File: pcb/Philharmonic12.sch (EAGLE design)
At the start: 47 parts, among them IC1 MC68B21, IC10 74LS74N, IC2 AY-3-8910-RP, IC3 AY-3-8910-RP, IC4 AY-3-8910-RP, IC5 AY-3-8910-RP, IC6 74LS138N, IC7 74LS30N, IC8 LM386N-1, IC9 LM386N-1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

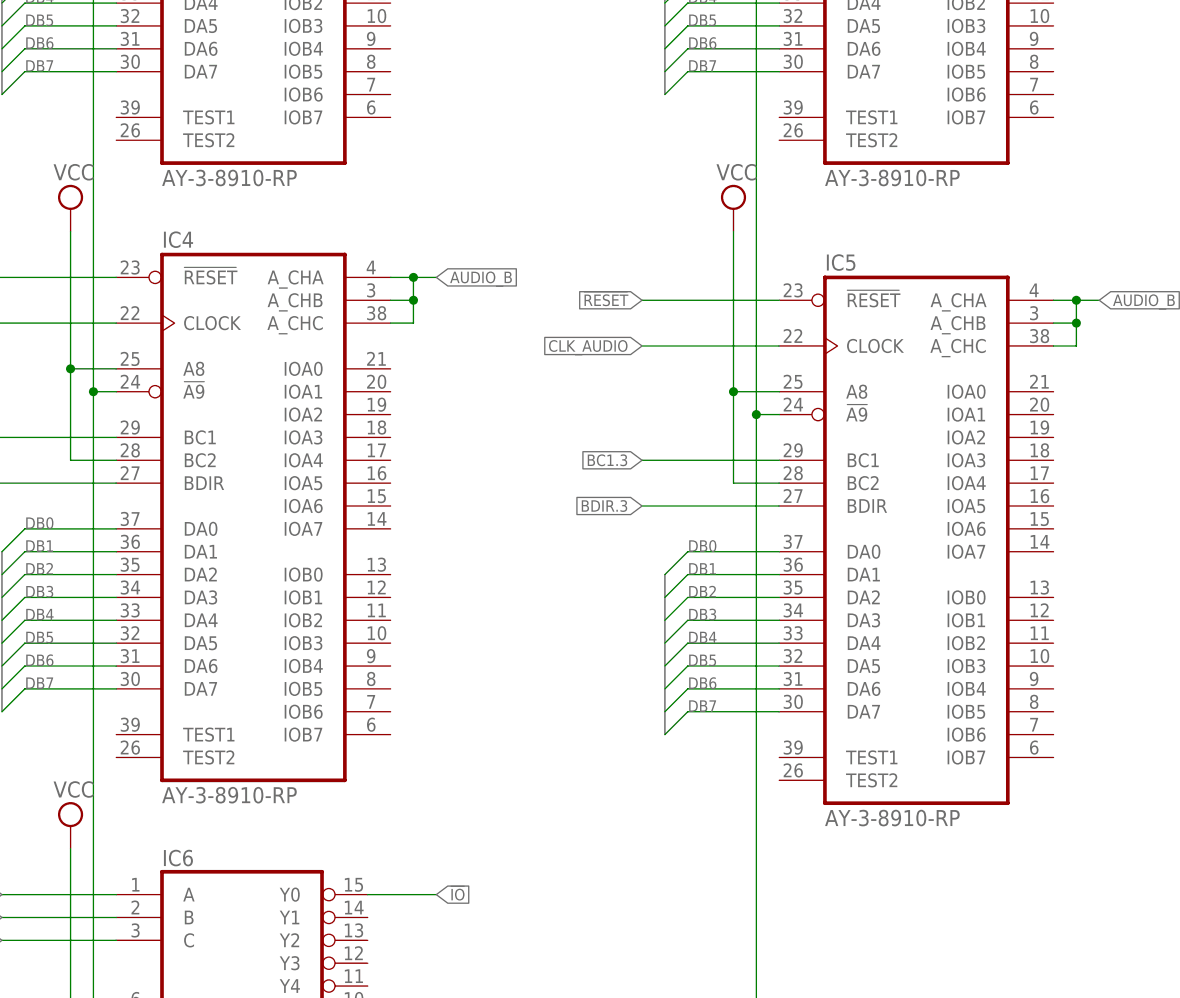
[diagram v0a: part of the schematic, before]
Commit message: Small dimension updates
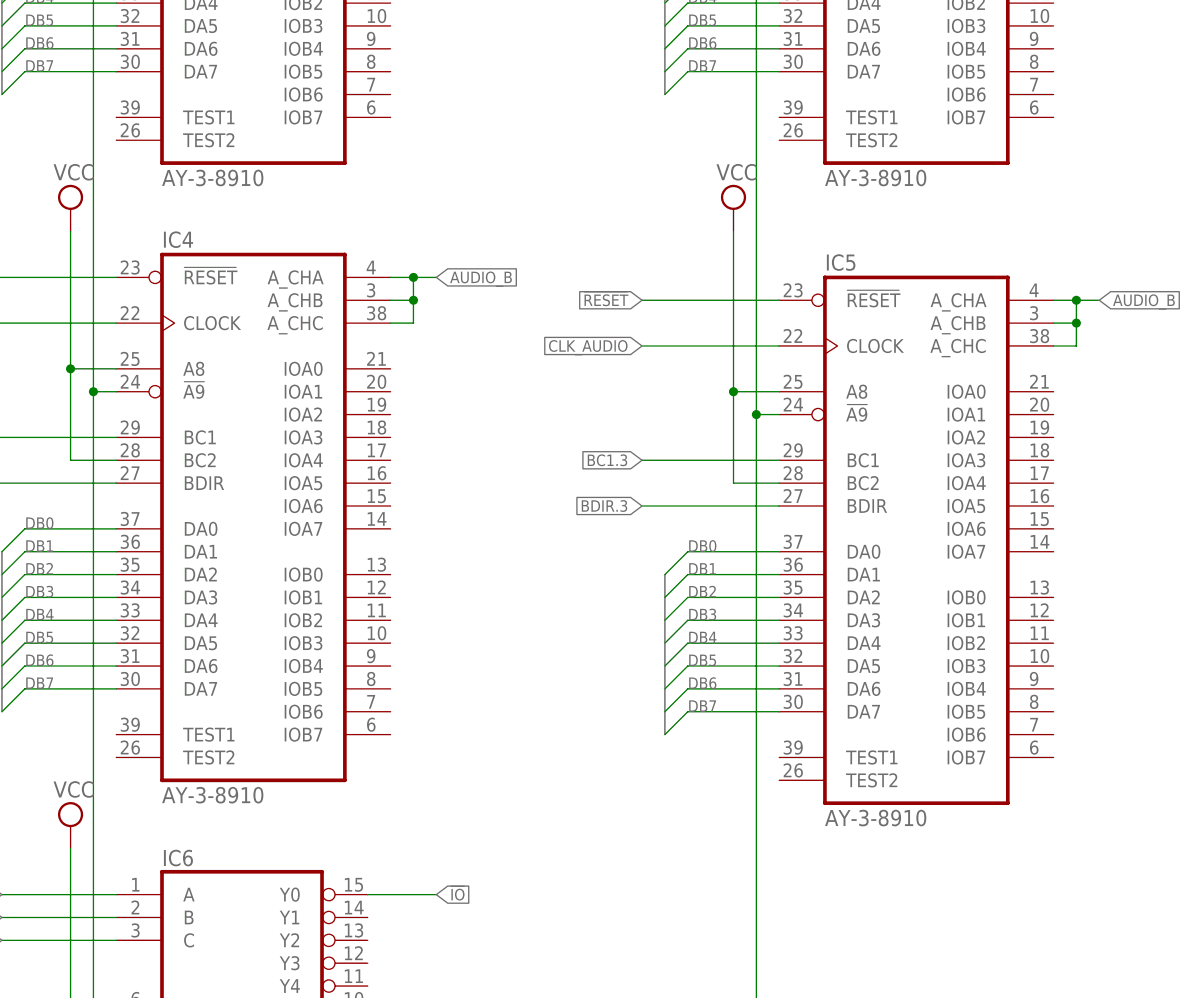
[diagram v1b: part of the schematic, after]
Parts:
- IC2, IC3, IC4, IC5: value AY-3-8910-RP -> AY-3-8910
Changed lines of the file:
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@@
 <parts>
 <part name="IC1" library="micro-motorola" deviceset="6821" device="R" value="MC68B21"/>
-<part name="IC2" library="general-instrument" deviceset="AY-3-8910" device="-RP"/>
-<part name="IC3" library="general-instrument" deviceset="AY-3-8910" device="-RP"/>
-<part name="IC4" library="general-instrument" deviceset="AY-3-8910" device="-RP"/>
-<part name="IC5" library="general-instrument" deviceset="AY-3-8910" device="-RP"/>
+<part name="IC2" library="general-instrument" deviceset="AY-3-8910" device="-RP" value="AY-3-8910"/>
+<part name="IC3" library="general-instrument" deviceset="AY-3-8910" device="-RP" value="AY-3-8910"/>
+<part name="IC4" library="general-instrument" deviceset="AY-3-8910" device="-RP" value="AY-3-8910"/>
+<part name="IC5" library="general-instrument" deviceset="AY-3-8910" device="-RP" value="AY-3-8910"/>
 <part name="X1" library="coco" deviceset="EXPANSION_PORT_COCO" device=""/>
 <part name="IC6" library="74xx-us-jlb" deviceset="74*138" device="N" technology="LS"/>

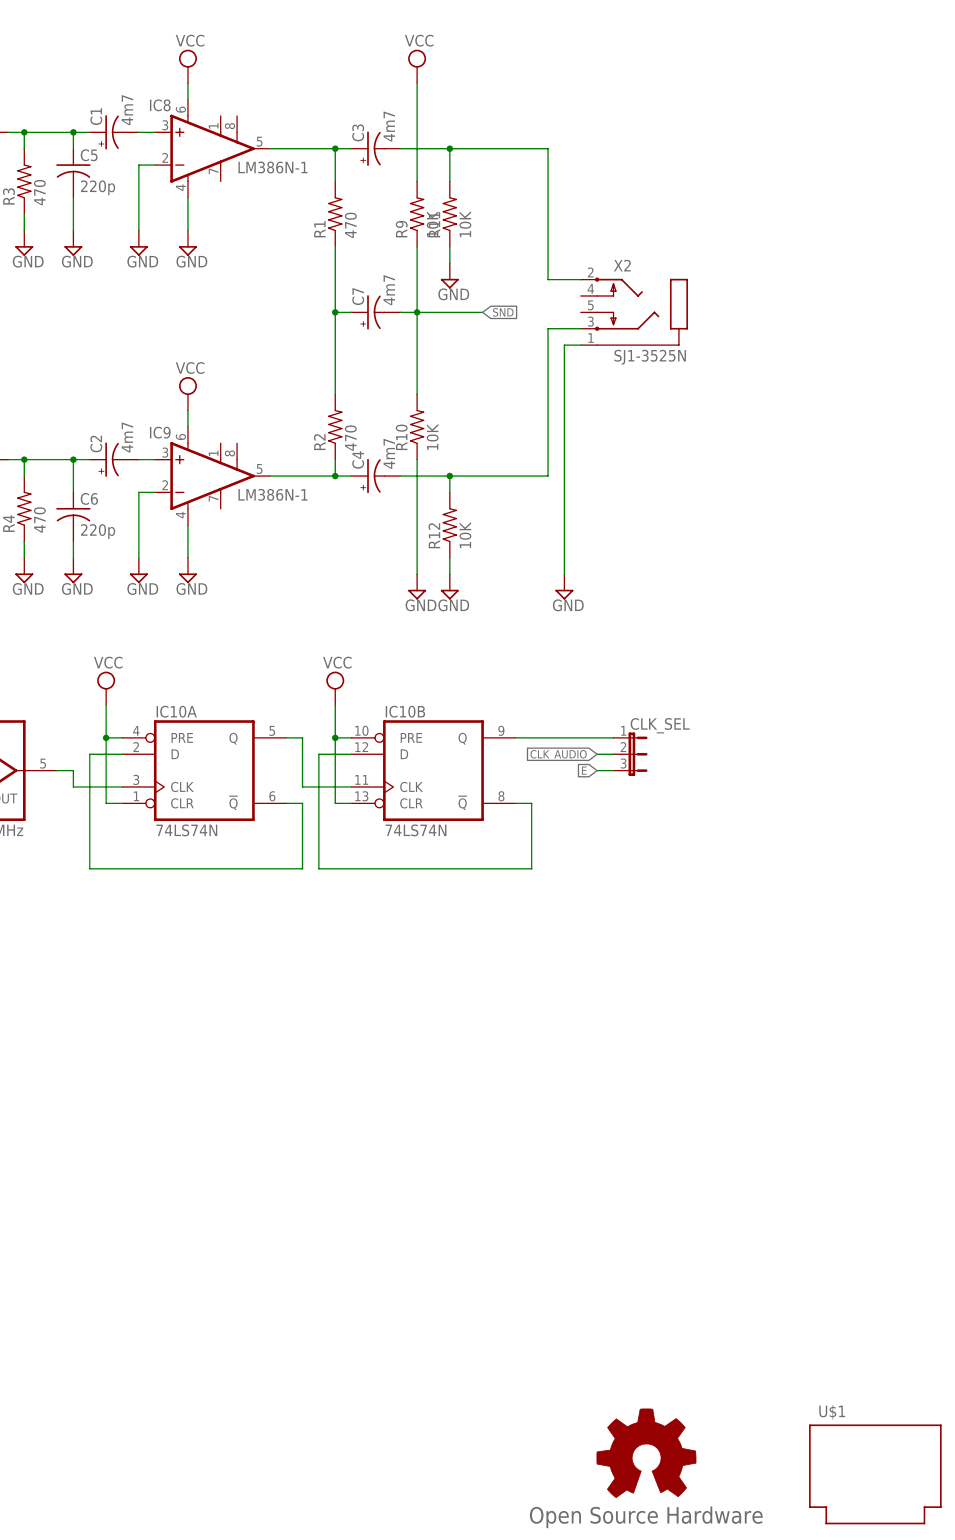
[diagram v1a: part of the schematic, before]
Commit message: Updates to schematic, Added BOM, and added sample code written by Chet Simpson
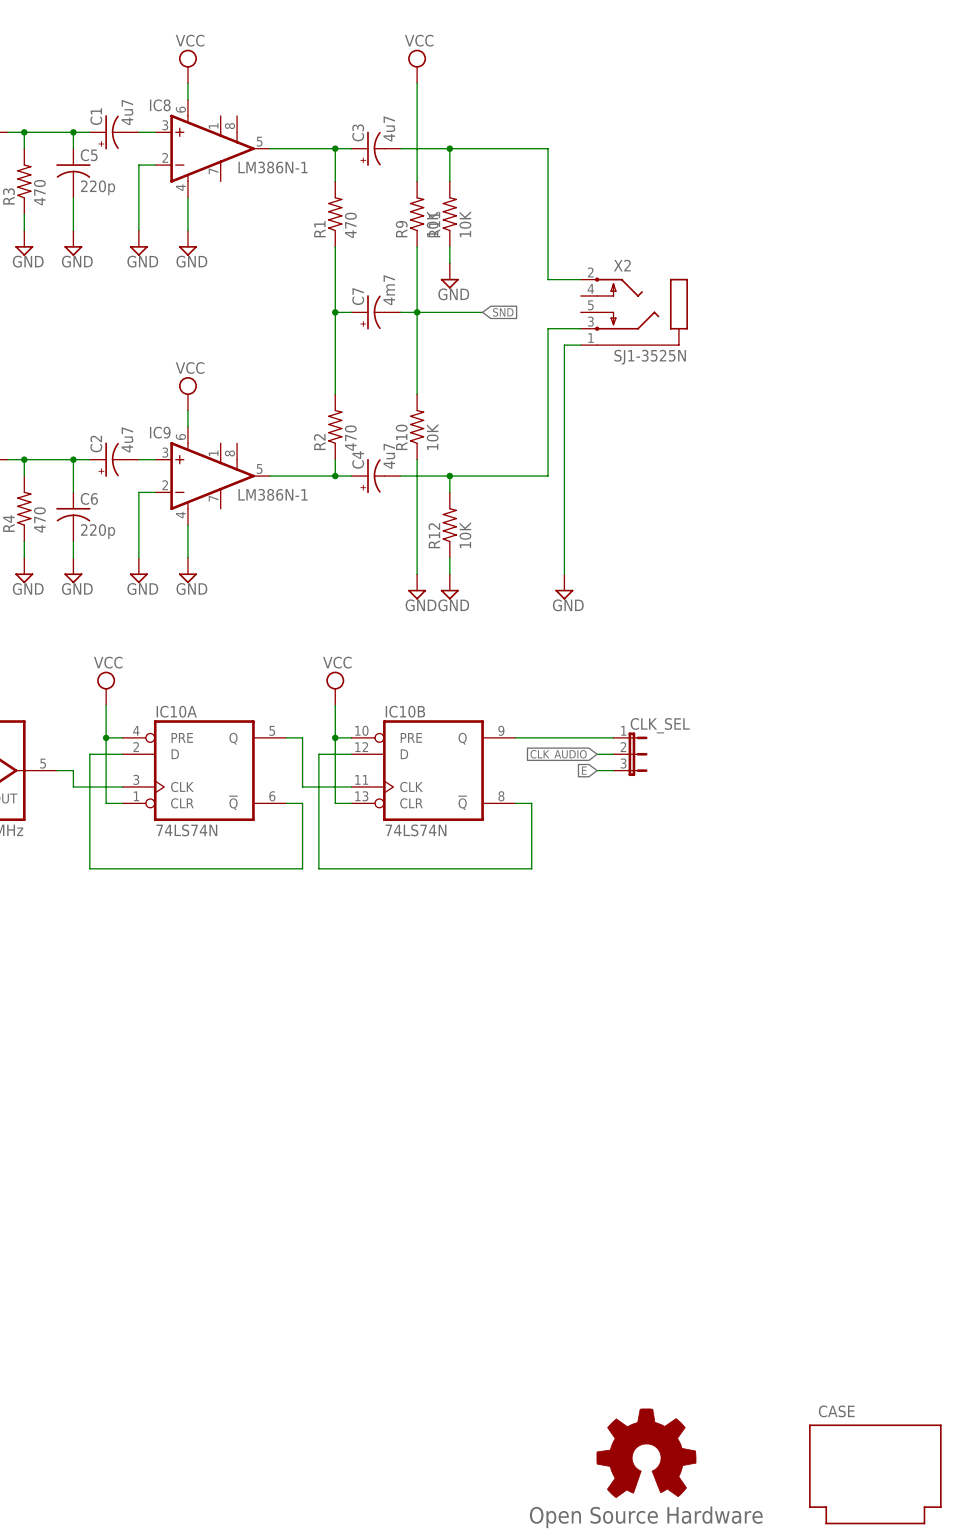
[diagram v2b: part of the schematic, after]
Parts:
- C1, C2, C3, C4: value 4m7 -> 4u7
- renumbered U$1 to CASE
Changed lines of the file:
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@@
 <part name="IC8" library="linear" deviceset="LM386?-*" device="N" technology="1"/>
 <part name="IC9" library="linear" deviceset="LM386?-*" device="N" technology="1"/>
-<part name="C1" library="rcl" deviceset="CPOL-US" device="E2.5-6" value="4m7"/>
-<part name="C2" library="rcl" deviceset="CPOL-US" device="E2.5-6" value="4m7"/>
+<part name="C1" library="rcl" deviceset="CPOL-US" device="E2.5-6" value="4u7"/>
+<part name="C2" library="rcl" deviceset="CPOL-US" device="E2.5-6" value="4u7"/>
 <part name="SUPPLY6" library="supply2" deviceset="GND" device=""/>
 <part name="SUPPLY7" library="supply2" deviceset="GND" device=""/>
@@
 <part name="R11" library="rcl" deviceset="R-US_" device="0204/7" value="10K"/>
 <part name="R12" library="rcl" deviceset="R-US_" device="0204/7" value="10K"/>
-<part name="C3" library="rcl" deviceset="CPOL-US" device="E2.5-6" value="4m7"/>
-<part name="C4" library="rcl" deviceset="CPOL-US" device="E2.5-6" value="4m7"/>
+<part name="C3" library="rcl" deviceset="CPOL-US" device="E2.5-6" value="4u7"/>
+<part name="C4" library="rcl" deviceset="CPOL-US" device="E2.5-6" value="4u7"/>
 <part name="C5" library="rcl" deviceset="C-US" device="025-025X050" value="220p"/>
 <part name="C6" library="rcl" deviceset="C-US" device="025-025X050" value="220p"/>
@@
 <part name="SUPPLY56" library="supply2" deviceset="GND" device=""/>
 <part name="SUPPLY57" library="supply2" deviceset="GND" device=""/>
-<part name="U$1" library="coco" deviceset="PROGRAM_PAK" device=""/>
+<part name="CASE" library="coco" deviceset="PROGRAM_PAK" device=""/>
 <part name="QG1" library="crystal" deviceset="QG5460" device="" value="3.579545MHz"/>
 <part name="SUPPLY58" library="supply2" deviceset="GND" device=""/>
@@
 <instance part="SUPPLY56" gate="GND" x="15.24" y="5.08"/>
 <instance part="SUPPLY57" gate="GND" x="10.16" y="5.08"/>
-<instance part="U$1" gate="A" x="416.56" y="45.72"/>
+<instance part="CASE" gate="A" x="416.56" y="45.72"/>
 <instance part="QG1" gate="1" x="276.86" y="154.94"/>
 <instance part="SUPPLY58" gate="GND" x="180.34" y="88.9"/>

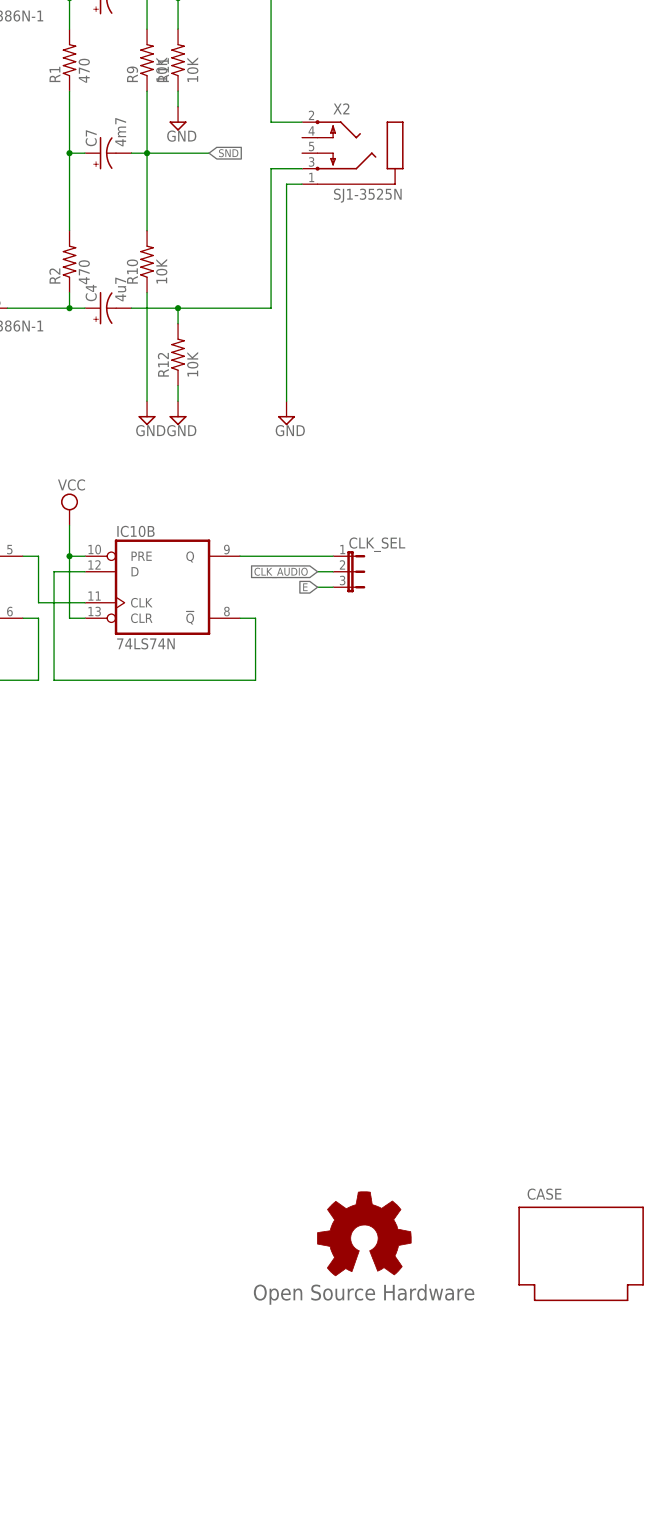
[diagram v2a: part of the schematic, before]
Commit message: Fix PCB legend placement error noted in Issue #1 (hexbus reported)
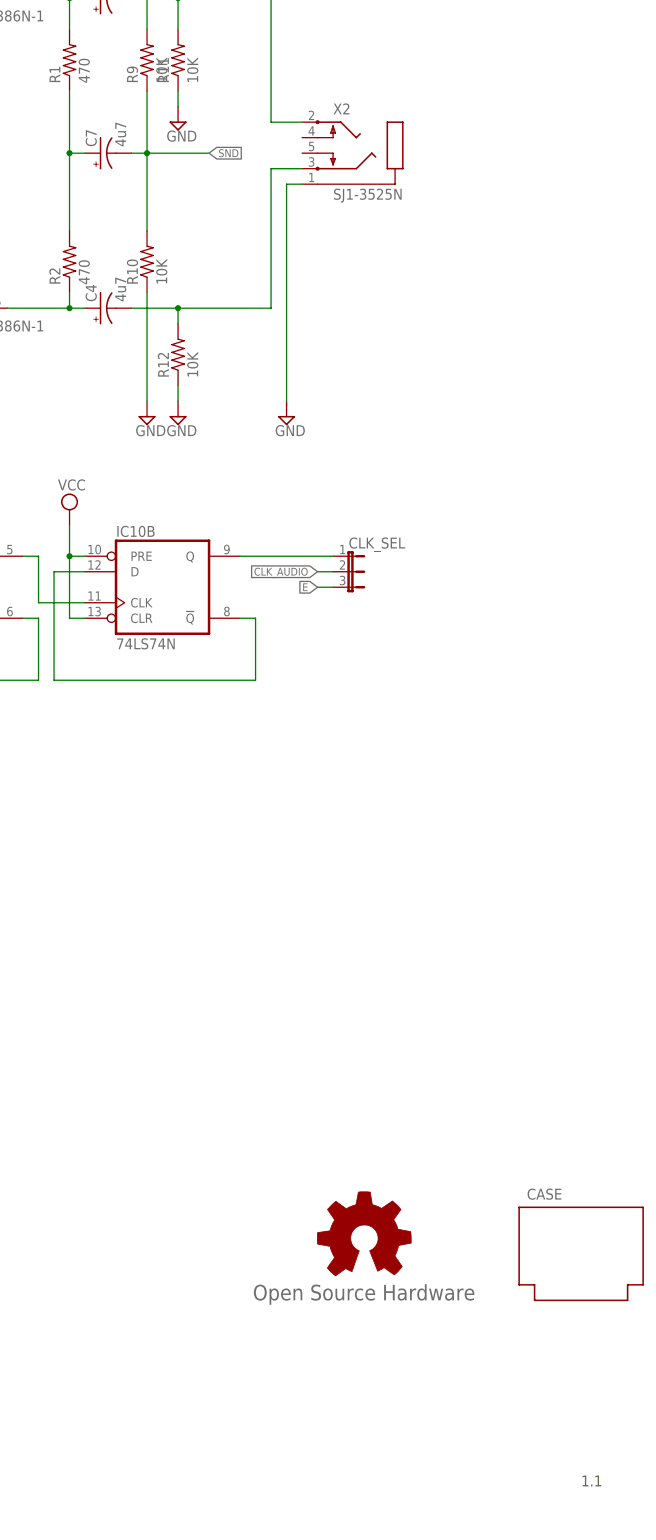
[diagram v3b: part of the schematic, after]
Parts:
- C7: value 4m7 -> 4u7
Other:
- note added: "1.1"
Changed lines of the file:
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@@
 <part name="SUPPLY16" library="supply2" deviceset="GND" device=""/>
 <part name="SUPPLY17" library="supply2" deviceset="GND" device=""/>
-<part name="C7" library="rcl" deviceset="CPOL-US" device="E2.5-6" value="4m7"/>
+<part name="C7" library="rcl" deviceset="CPOL-US" device="E2.5-6" value="4u7"/>
 <part name="SUPPLY18" library="supply2" deviceset="VCC" device=""/>
 <part name="SUPPLY19" library="supply2" deviceset="GND" device=""/>
@@
 <sheet>
 <plain>
+<text x="416.56" y="7.62" size="1.778" layer="97">1.1</text>
 </plain>
 <instances>
